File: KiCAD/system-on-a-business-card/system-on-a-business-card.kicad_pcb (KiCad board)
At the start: 2 copper layers, 85 x 54 mm, 84 parts, among them J1 USB_C_Receptacle, J2 X077-6428TSWCG01-H13, J3 Conn_01x04_Socket, J4 Micro_SD_Card, Q1 2N7002K, Q2 2N7002K, SW1 SW_Push, SW2 SW_Push, U1 USBLC6-2SC6, U2 ESP32-C3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

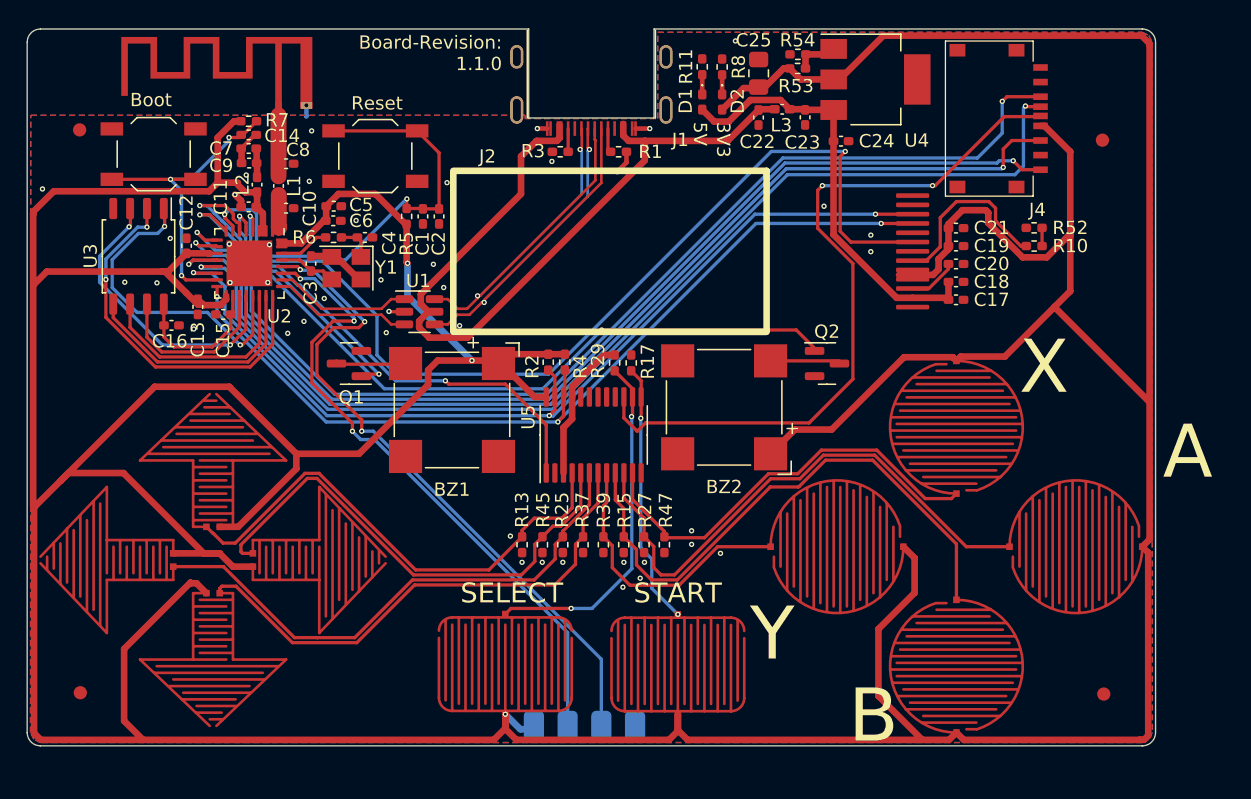
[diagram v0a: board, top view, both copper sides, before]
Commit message: #10: added pull-ups to SD-Card connection, tweaks in layout
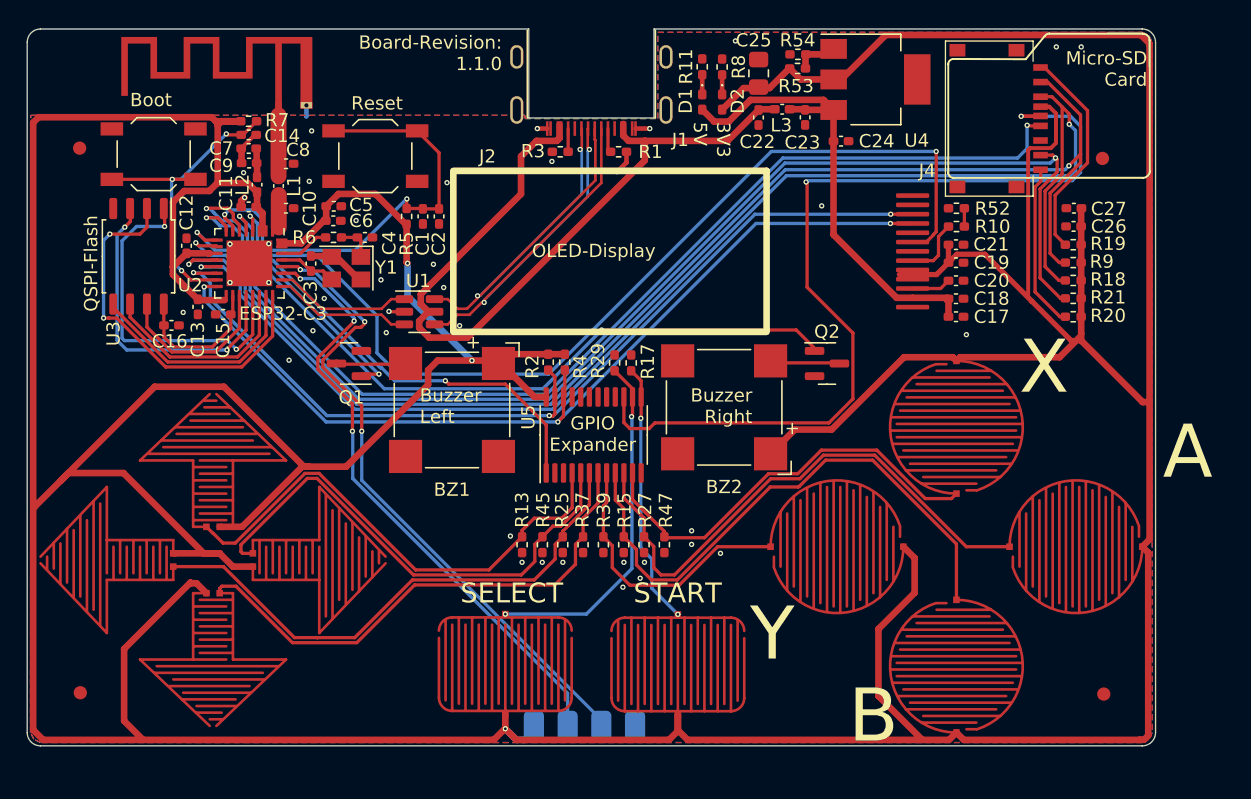
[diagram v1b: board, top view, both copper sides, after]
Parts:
- added C26: 10u, Capacitor_SMD:C_0402_1005Metric_Pad0.74x0.62mm_HandSolder, F.Cu at (156.3, 84.9)
- added C27: 100n, Capacitor_SMD:C_0402_1005Metric_Pad0.74x0.62mm_HandSolder, F.Cu at (156.3, 83.5)
- added R18: 47k, Resistor_SMD:R_0402_1005Metric_Pad0.72x0.64mm_HandSolder, F.Cu at (156.3, 88.9)
- added R19: 47k, Resistor_SMD:R_0402_1005Metric_Pad0.72x0.64mm_HandSolder, F.Cu at (156.3, 86.2)
- added R20: 47k, Resistor_SMD:R_0402_1005Metric_Pad0.72x0.64mm_HandSolder, F.Cu at (156.3, 91.7)
- added R21: 47k, Resistor_SMD:R_0402_1005Metric_Pad0.72x0.64mm_HandSolder, F.Cu at (156.3, 90.3)
- added R9: 47k, Resistor_SMD:R_0402_1005Metric_Pad0.72x0.64mm_HandSolder, F.Cu at (156.3, 87.6)
- moved R52 6.04 mm to (147.5, 83.5)
- moved R10 6.03 mm to (147.5, 84.9)
- moved FID1 1.38 mm to (158.5, 79.8)
- moved FID3 1.38 mm to (81.5, 79.0)
- moved C17 1.27 mm to (147.5, 91.7)
- moved C18 1.27 mm to (147.5, 90.3)
- moved C20 1.26 mm to (147.5, 89.0)
- moved C19 1.25 mm to (147.5, 87.6)
- moved C21 1.25 mm to (147.5, 86.2)
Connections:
- J4 pad 1: unconnected-(J4-DAT2-Pad1) -> Net-(J4-DAT2)
- J4 pad 10: unconnected-(J4-SHIELD-Pad10) -> GND
- J4 pad 2: unconnected-(J4-DAT3/CD-Pad2) -> SS
- J4 pad 3: MTMS -> MOSI
- J4 pad 4: MTDO -> +3.3V
- J4 pad 5: +3.3V -> SCK
- J4 pad 6: MTCK -> GND
- J4 pad 7: GND -> MISO
- J4 pad 8: MTDI -> Net-(J4-DAT1)
- U2 pad 10: MTDI -> MISO
- U2 pad 12: MTCK -> SS
- U2 pad 13: MTDO -> MOSI
- U2 pad 9: MTMS -> SCK
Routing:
- net MOSI: track 0.00 -> 101.2 mm, vias 0 -> 2
- net SS: track 0.00 -> 99.2 mm, vias 0 -> 2
- net MISO: track 0.00 -> 92.8 mm, vias 0 -> 2
- net MTMS: track 82.7 -> 0.00 mm, vias 2 -> 0
- net MTDO: track 82.6 -> 0.00 mm, vias 2 -> 0
- net MTCK: track 81.7 -> 0.00 mm, vias 2 -> 0
- net SCK: track 0.00 -> 80.2 mm, vias 0 -> 2
- net MTDI: track 79.6 -> 0.00 mm, vias 2 -> 0
- net Net-(J4-DAT2): track 0.00 -> 16.0 mm
- net /Host/SDcard_DET: track 55.3 -> 70.1 mm
- net Net-(J4-DAT1): track 0.00 -> 12.4 mm
- net GND: track 24.9 -> 12.5 mm, vias 43 -> 40
- net +3.3V: track 482.2 -> 494.1 mm
- net Net-(J2-Pin_6): track 13.6 -> 3.57 mm
- net +5V: track 32.7 -> 35.9 mm
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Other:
- board text added: "Buzzer Left"
- board text added: "Buzzer Right"
- board text added: "ESP32-C3"
- board text added: "GND"
- board text added: "GPIO Expander"
- board text added: "Micro-SD Card"
- board text added: "OLED-Display"
- board text added: "QSPI-Flash"
- board text added: "RXD"
- board text added: "TXD"

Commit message: #10: connected display reset to GPIO Expander
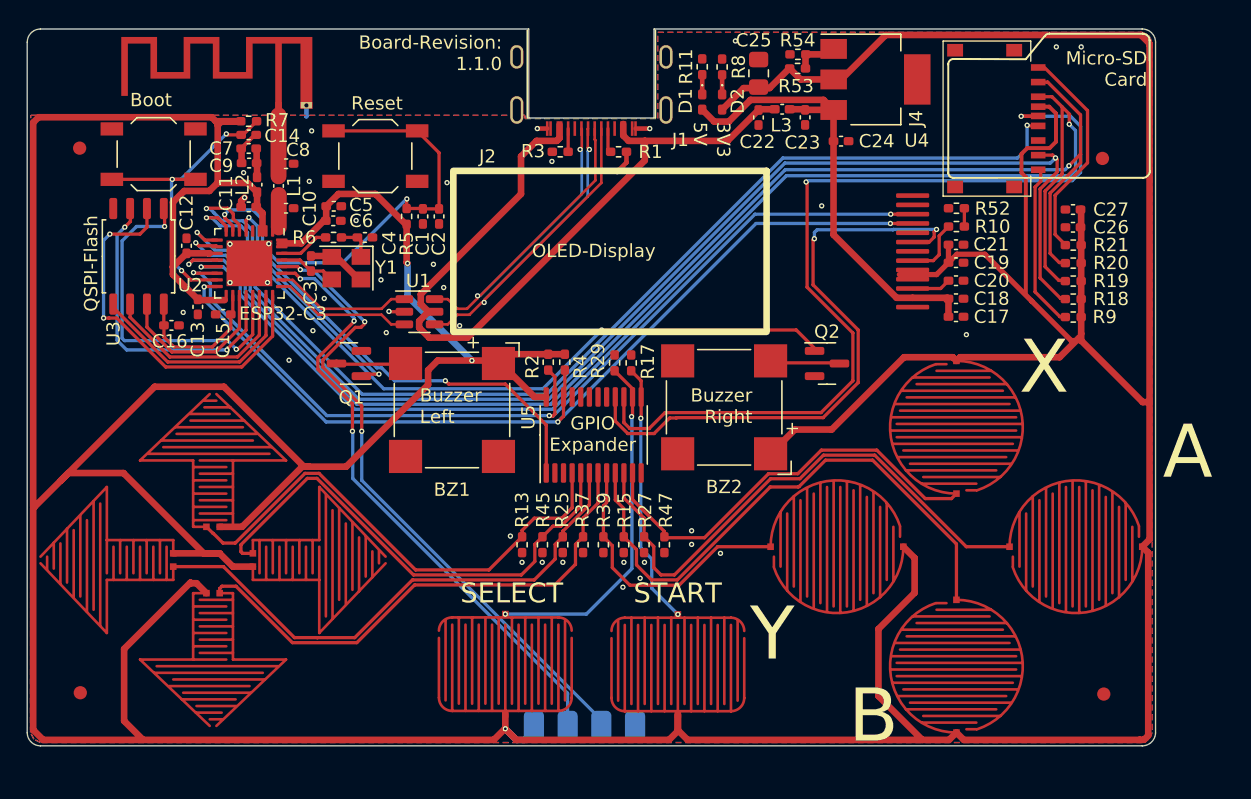
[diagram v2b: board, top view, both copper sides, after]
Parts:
- moved R9 4.10 mm to (156.3, 91.7)
- moved R20 4.04 mm to (156.3, 87.6)
- moved R21 4.01 mm to (156.3, 86.3)
- moved R19 2.74 mm to (156.3, 89.0)
- moved R18 1.40 mm to (156.3, 90.3)
- moved J4 0.18 mm to (153.1, 76.8)
- moved C27 0.12 mm to (156.3, 83.6)
- moved C26 0.08 mm to (156.3, 84.9)
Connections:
- net /Host/SDcard_DET renamed /Resistive Touch Circuit/SDCard_DET
- net SCK renamed /Host/SCK
- J4 pad 2: SS -> /Host/SS
- J4 pad 3: MOSI -> /Host/MOSI
- J4 pad 7: MISO -> /Host/MISO
- R18 pad 2: MOSI -> /Host/MISO
- R19 pad 2: Net-(J4-DAT2) -> /Host/MOSI
- R20 pad 2: Net-(J4-DAT1) -> /Host/SS
- R21 pad 2: MISO -> Net-(J4-DAT2)
- R9 pad 2: SS -> Net-(J4-DAT1)
- U2 pad 10: MISO -> /Host/MISO
- U2 pad 12: SS -> /Host/SS
- U2 pad 13: MOSI -> /Host/MOSI
- U2 pad 4: /Display Circuit/RESET_DISPLAY -> unconnected-(U2-XTAL_32K_P/ADC1_CH0-Pad4)
- U5 pad 16: unconnected-(U5-P13-Pad16) -> /Display Circuit/RESET_DISPLAY
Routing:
- net MOSI: track 101.2 -> 0.00 mm, vias 2 -> 0
- net /Host/MOSI: track 0.00 -> 101.2 mm, vias 0 -> 2
- net SS: track 99.2 -> 0.00 mm, vias 2 -> 0
- net /Host/SS: track 0.00 -> 99.2 mm, vias 0 -> 2
- net MISO: track 92.8 -> 0.00 mm, vias 2 -> 0
- net /Host/MISO: track 0.00 -> 92.8 mm, vias 0 -> 2
- net /Display Circuit/RESET_DISPLAY: track 75.7 -> 47.2 mm
- net /Host/IO_EXP_INT: track 35.5 -> 34.6 mm
- net /Resistive Touch Circuit/SDCard_DET: track 70.1 -> 69.3 mm
- net RESET: track 35.4 -> 36.2 mm

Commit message: #10: mintor tweaks in routing, removed fiducials from bom, added values to buzzer and sd-card slot
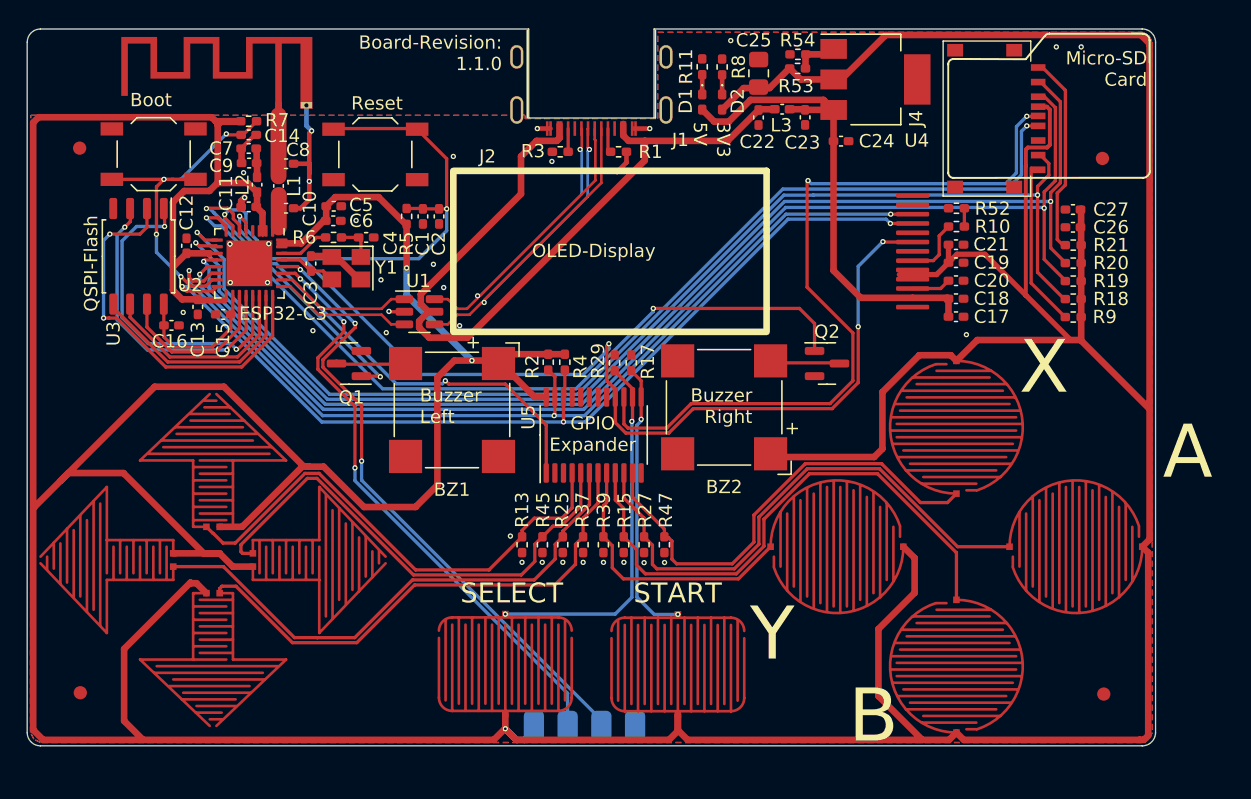
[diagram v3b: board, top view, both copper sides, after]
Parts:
- BZ1, BZ2: value Buzzer -> MLT-7525
- D1, D2: value LED -> XL-1005UGC
- J4: value Micro_SD_Card -> TF-018B-H15
- moved SW1 0.12 mm to (103.7, 79.5)
- moved C4 0.09 mm to (103.0, 85.7)
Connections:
- J2 pad 8: /Display Circuit/RESET_DISPLAY -> RESET
- U5 pad 16: /Display Circuit/RESET_DISPLAY -> RESET
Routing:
- net RESET: track 36.2 -> 107.1 mm, vias 2 -> 5
- net /Display Circuit/RESET_DISPLAY: track 47.2 -> 0.00 mm, vias 2 -> 0
- net /Resistive Touch Circuit/SDCard_DET: track 69.3 -> 59.0 mm
- net GND: track 12.5 -> 22.8 mm, vias 40 -> 35
- net /Host/MOSI: track 101.2 -> 91.7 mm
- net +3.3V: track 494.6 -> 502.8 mm
- net /Host/SS: track 99.2 -> 91.6 mm
- net /Display Circuit/SCL: track 69.5 -> 72.6 mm
- net X: track 32.1 -> 35.1 mm
- net /Host/MISO: track 92.8 -> 89.8 mm
- net BUZZER_R: track 56.5 -> 58.7 mm
- net UART_TXD: track 48.9 -> 46.9 mm
- net BOOT: track 24.6 -> 26.5 mm, vias 3 -> 4
- net /Host/SCK: track 80.2 -> 81.9 mm
- net +5V: track 35.9 -> 37.5 mm
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
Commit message: #10: fixed wiring for display reset
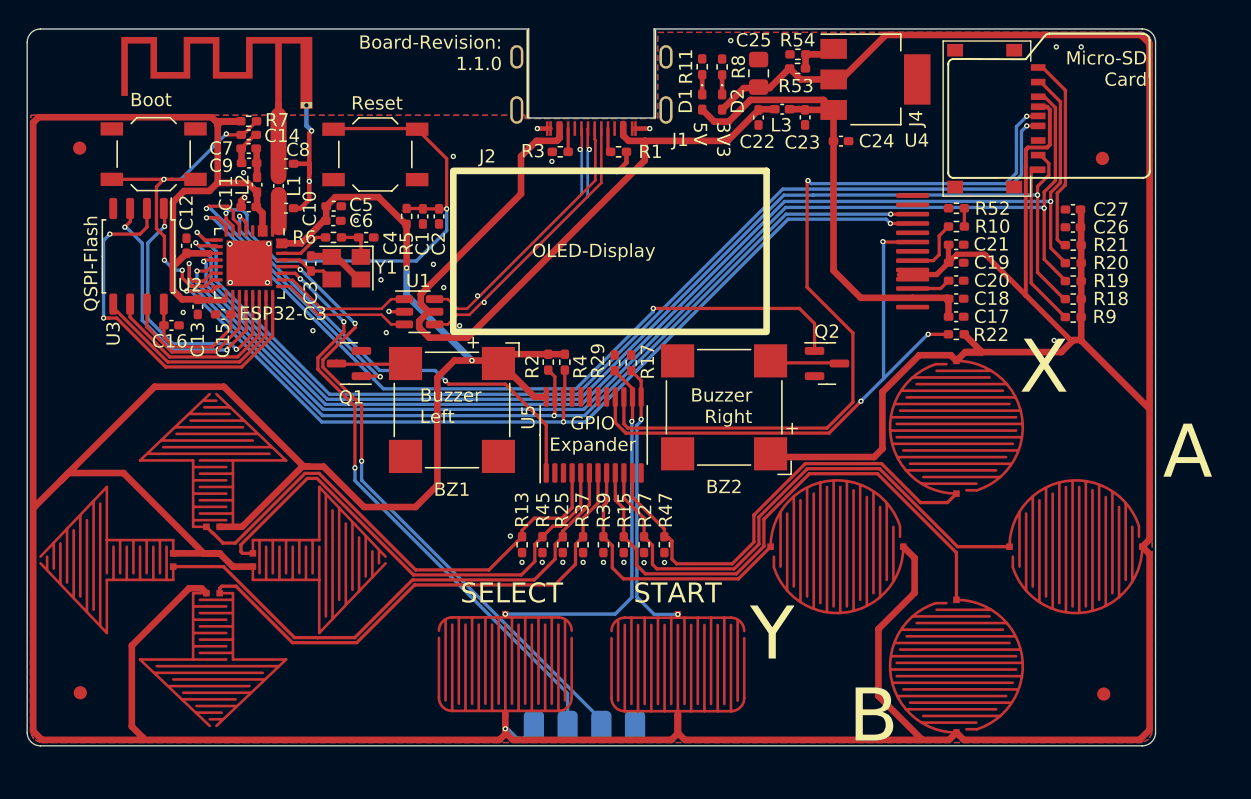
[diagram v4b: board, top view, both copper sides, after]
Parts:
- added R22: 5k1, Resistor_SMD:R_0402_1005Metric_Pad0.72x0.64mm_HandSolder, F.Cu at (147.5, 93.0)
- R53: value 121 -> 121R
- R54: value 75 -> 75R
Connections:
- J2 pad 8: RESET -> RESET_DISPLAY
- U5 pad 16: RESET -> RESET_DISPLAY
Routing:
- net RESET: track 107.1 -> 39.4 mm, vias 5 -> 2
- net RESET_DISPLAY: track 0.00 -> 43.0 mm, vias 0 -> 3
- net Net-(U2-SPICS0/GPIO14): track 24.9 -> 21.0 mm
- net +3.3V: track 502.8 -> 505.5 mm
- net Net-(U2-SPIWP/GPIO13): track 22.7 -> 21.2 mm
- net /Display Circuit/SDA: track 72.5 -> 73.6 mm
- net /Display Circuit/SCL: track 72.6 -> 71.6 mm
- net /Resistive Touch Circuit/SDCard_DET: track 59.0 -> 59.9 mm
- net /Host/IO_EXP_INT: track 35.8 -> 35.2 mm

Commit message: #10: minor tweaks
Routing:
- net +3.3V: track 505.5 -> 503.3 mm
- added copper zone on F.Cu, net +3.3V
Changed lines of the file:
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@@
   (segment (start 92.15 76.94875) (end 93.585 76.94875) (width 0.5) (layer "F.Cu") (net 5))
   (segment (start 126.515649 123.027649) (end 126.515649 121.640947) (width 0.5) (layer "F.Cu") (net 5))
+  (segment (start 146.004375 88.5) (end 145.375 88.5) (width 0.4) (layer "F.Cu") (net 5))
   (segment (start 133.744 102.244) (end 141.306 102.244) (width 0.5) (layer "F.Cu") (net 5))
-  (segment (start 146.004375 88.5) (end 143.2 88.5) (width 0.4) (layer "F.Cu") (net 5))
   (segment (start 100.0225 83.35) (end 100.0225 84.4175) (width 0.5) (layer "F.Cu") (net 5))
   (segment (start 152.73 80.300486) (end 152.727 80.303486) (width 0.3) (layer "F.Cu") (net 5))
@@
   (segment (start 89.323 82.202) (end 91.223 82.202) (width 0.5) (layer "F.Cu") (net 5))
   (segment (start 91.85 77.24875) (end 92.15 76.94875) (width 0.5) (layer "F.Cu") (net 5))
-  (segment (start 146.9 87.604375) (end 146.004375 88.5) (width 0.4) (layer "F.Cu") (net 5))
   (segment (start 141.925 101.625) (end 141.925 97.35) (width 0.5) (layer "F.Cu") (net 5))
   (segment (start 113.515649 122.715649) (end 113.515649 121.619501) (width 0.5) (layer "F.Cu") (net 5))
@@
   (segment (start 154.333 78.927) (end 152.8778 78.927) (width 0.3) (layer "F.Cu") (net 5))
   (segment (start 144.925 123.55) (end 141.625 120.25) (width 0.5) (layer "F.Cu") (net 5))
+  (segment (start 146.9 87.604375) (end 146.004375 88.5) (width 0.4) (layer "F.Cu") (net 5))
   (segment (start 144.925 123.55) (end 127.038 123.55) (width 0.5) (layer "F.Cu") (net 5))
   (segment (start 91.402 76.648) (end 91.70275 76.94875) (width 0.5) (layer "F.Cu") (net 5))
@@
       )
     )
+  )
+  (zone (net 5) (net_name "+3.3V") (layer "F.Cu") (hatch edge 0.5)
+    (priority 1)
+    (connect_pads yes (clearance 0))
+    (min_thickness 0.25) (filled_areas_thickness no)
+    (fill yes (thermal_gap 0.5) (thermal_bridge_width 0.5))
+    (polygon
+      (pts
+        (xy 142.95 88.05)
+        (xy 143.025 87.975)
+        (xy 145.35 87.975)
+        (xy 145.45 88.05)
+        (xy 145.45 88.925)
+        (xy 145.35 89.025)
+        (xy 143.05 89.025)
+        (xy 142.95 88.925)
+        (xy 142.95 88.85)
+      )
+    )
